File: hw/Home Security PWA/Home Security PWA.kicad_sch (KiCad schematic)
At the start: 52 parts, among them J1 Conn_01x10_Pin, J10 1825960000, J11 1825960000, J12 1825960000, J13 1825960000, J14 1825960000, J15 1825960000, J16 1825960000, J17 1825960000, J18 1825960000, J19 1825960000, J2 Conn_01x10_Pin, J20 1825960000, J21 1825960000, J22 1825960000, J23 1825960000, J24 1825960000, J25 1825960000, J26 1825960000, J27 1825960000, J28 1825960000, J29 1825960000, J3 1825960000, J30 1825960000, J31 1825960000, J32 1825960000, J33 1825960000, J34 1825960000, J4 1825960000, J5 1825960000, J6 1825960000, J7 1825960000, J8 1825960000, J9 1825960000, U1 ADS1115IDGS, U2 ADS1115IDGS, U3 MCP23017_SO

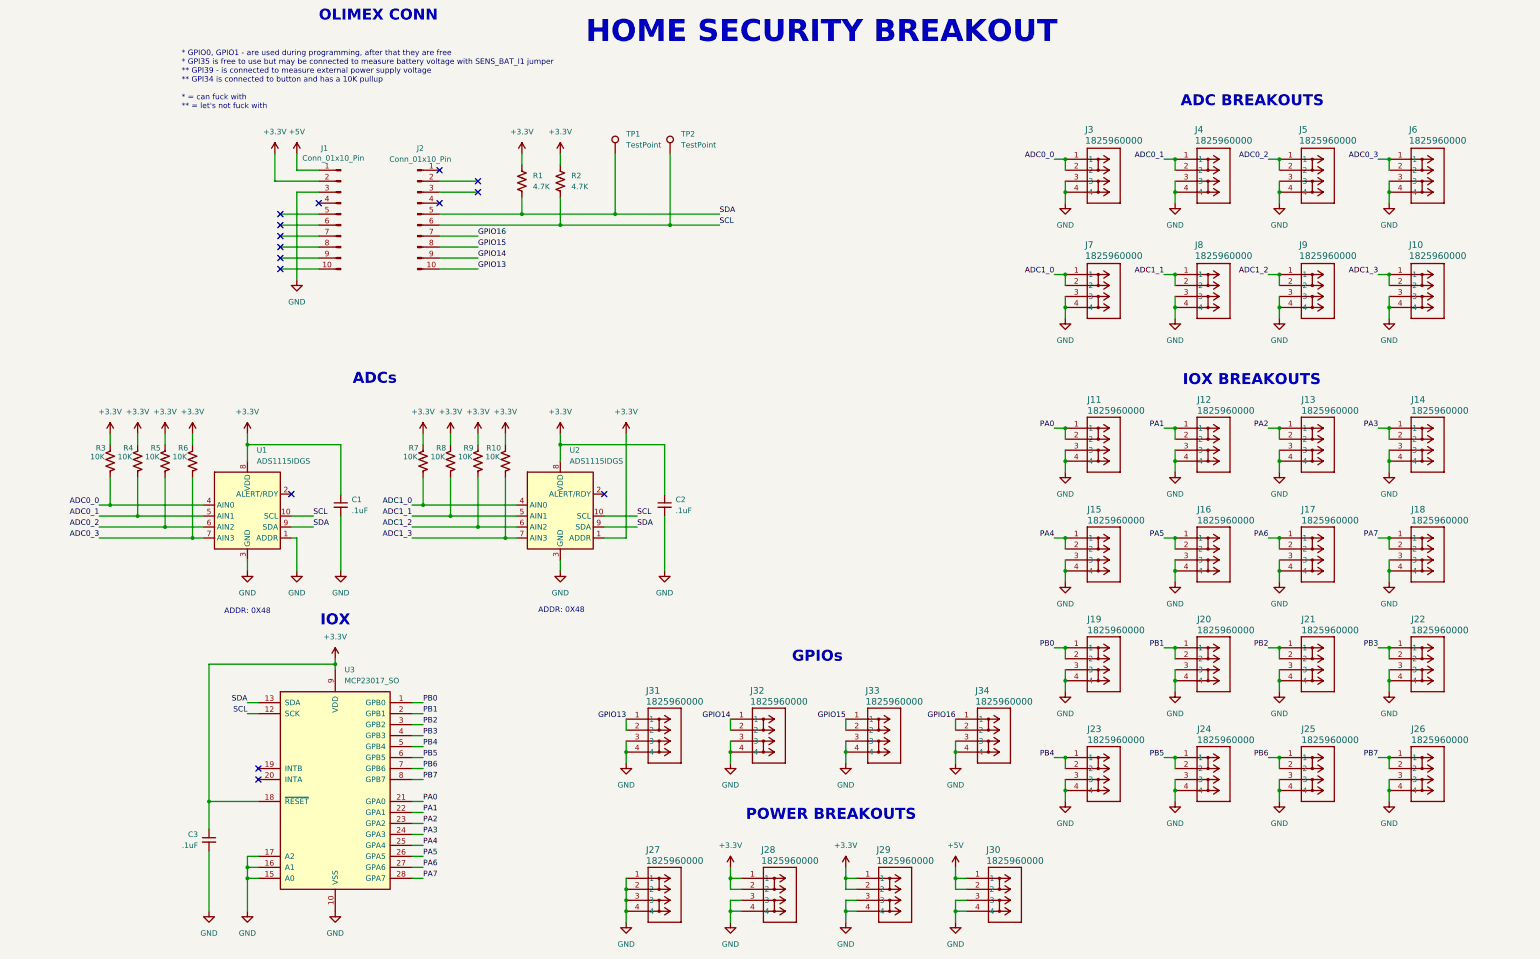
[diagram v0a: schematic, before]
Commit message: Remove these "per project" components.
Updates to Home Security with Inventree, new symbols, new schematics.
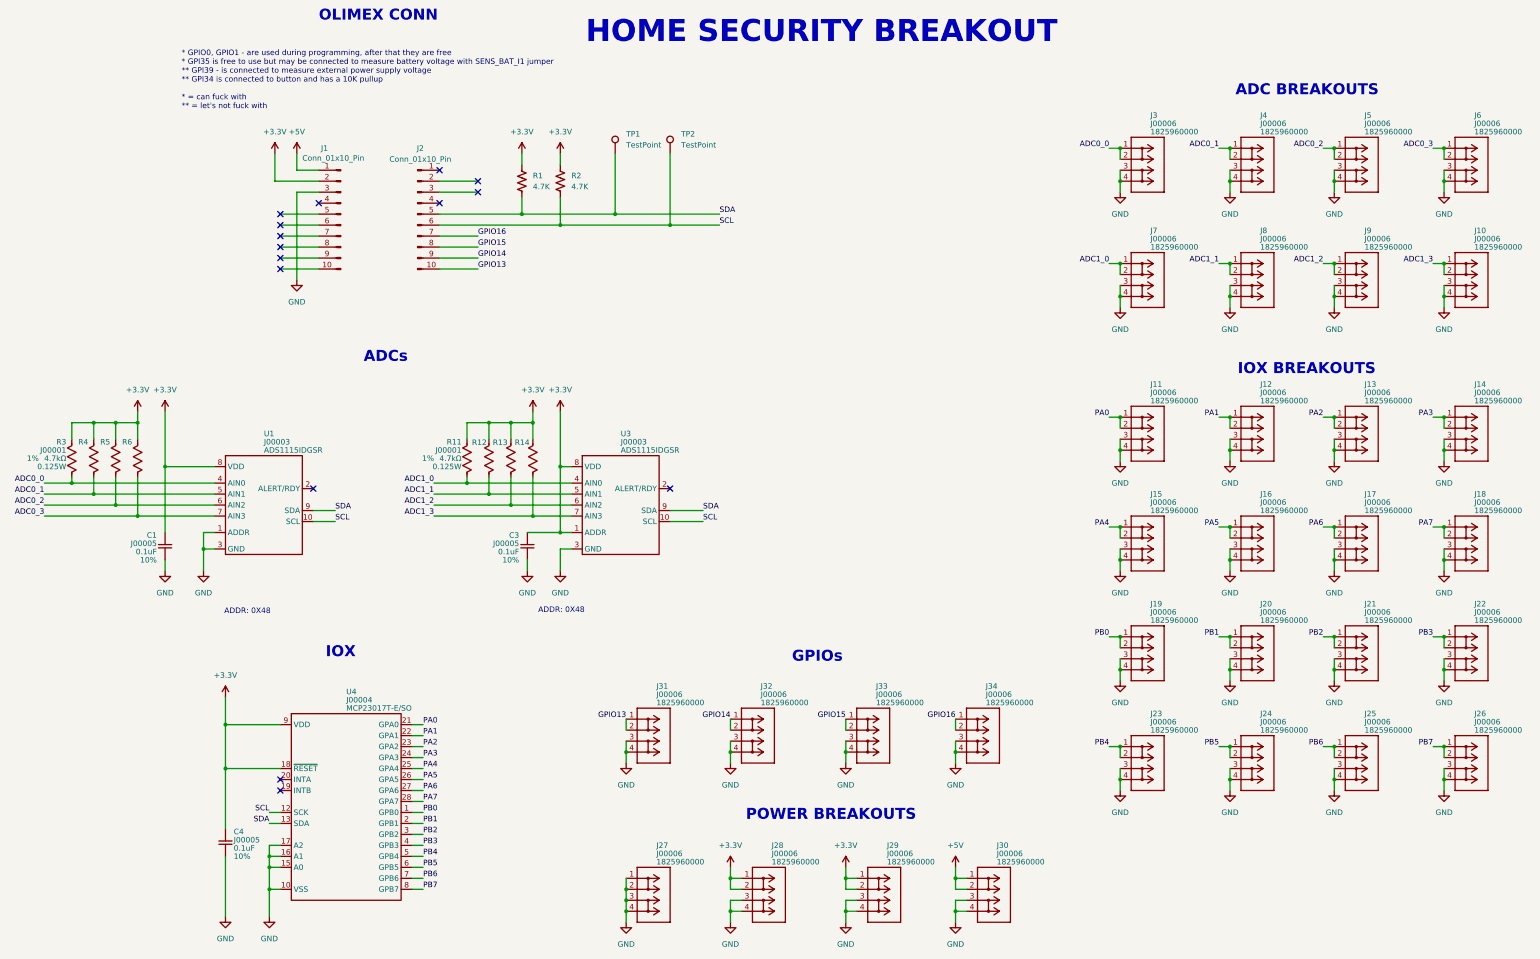
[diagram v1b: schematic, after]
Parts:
- removed C1, C2, C3: .1uF, Capacitor_SMD:C_0805_2012Metric_Pad1.18x1.45mm_HandSolder, symbol Device:C_Small
- removed R10, R7, R8, R9: 10K, Resistor_SMD:R_0805_2012Metric_Pad1.20x1.40mm_HandSolder, symbol Device:R_US
- removed U1, U2: ADS1115IDGS, Package_SO:TSSOP-10_3x3mm_P0.5mm, symbol Analog_ADC:ADS1115IDGS
- removed U3: MCP23017_SO, Package_SO:SOIC-28W_7.5x17.9mm_P1.27mm, symbol Interface_Expansion:MCP23017_SO
- added C1, C3, C4: J00005, JLibrary:CAPC201X125X100L50M, symbol JLibrary_inventree:J00005
- added R11, R12, R13, R14: J00001, JLibrary:RESC2012X60M, symbol JLibrary_inventree:J00001
- added U1, U3: J00003, JLibrary:SOP10P50_300X490X110L55X22M, symbol JLibrary_inventree:J00003
- added U4: J00004, JLibrary:SOIC127P1030X265-28M, symbol JLibrary_inventree:J00004
- J10, J11, J12, J13, J14, J15, J16, J17, J18, J19, J20, J21, J22, J23, J24, J25, J26, J27, J28, J29, J3, J30, J31, J32, J33, J34, J4, J5, J6, J7, J8, J9: value 1825960000 -> J00006; footprint footprint:CONN_1825960000_WED -> JLibrary:J00006; symbol 1825960000:1825960000 -> JLibrary_inventree:J00006; Current (none) -> 12A; Gender (none) -> Female; InvenTree (none) -> 20; MPN_1 (none) -> 1825960000; Manufacturer_1 (none) -> Weidmüller; Mount (none) -> TH; Orientation (none) -> Vertical; Part URL (none) -> https://inventree.justyn.party/web/part/20/; Pin Arrangement (none) -> 1x2; SPN_1_1 (none) -> 281-2124-ND; Supplier_1_1 (none) -> Digikey; TMax (none) -> 120C; TMin (none) -> -50C; Voltage (none) -> 300V
- R3, R4, R5, R6: value 10K -> J00001; footprint Resistor_SMD:R_0805_2012Metric_Pad1.20x1.40mm_HandSolder -> JLibrary:RESC2012X60M; symbol Device:R_US -> JLibrary_inventree:J00001; InvenTree (none) -> 15; MPN_1 (none) -> CRCW08054K70FKEAC; Manufacturer_1 (none) -> Vishay Dale; Mount (none) -> SM; Package (none) -> 0805; Part URL (none) -> https://inventree.justyn.party/web/part/15/; Power (none) -> 0.125W; Resistance (none) -> 4.7kΩ; SPN_1_1 (none) -> 541-4131-1-ND; SPN_1_2 (none) -> 541-4131-2-ND; Supplier_1_1 (none) -> Digikey; Supplier_1_2 (none) -> Digikey; TMax (none) -> 155C; TMin (none) -> -55C; Tolerance (none) -> 1%; Voltage (none) -> 150V
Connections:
- net +3.3V: now also C1.1, C3.1, C4.1, U1.8 (VDD), U3.1 (ADDR), U3.8 (VDD), U4.18 (~{RESET}), U4.9 (VDD); no longer R3.1, R4.1, R5.1, R6.1
- net ADC0_0: now also U1.4 (AIN0); no longer R3.2
- net ADC0_1: now also U1.5 (AIN1); no longer R4.2
- net ADC0_2: now also U1.6 (AIN2); no longer R5.2
- net ADC0_3: now also U1.7 (AIN3); no longer R6.2
- net ADC1_0: now also U3.4 (AIN0)
- net ADC1_1: now also U3.5 (AIN1)
- net ADC1_2: now also U3.6 (AIN2)
- net ADC1_3: now also U3.7 (AIN3)
- net GND: now also C1.2, C3.2, C4.2, U1.1 (ADDR), U1.3 (GND), U3.3 (GND), U4.10 (VSS), U4.15 (A0), U4.16 (A1), U4.17 (A2)
- net PA0: now also U4.21 (GPA0)
- net PA1: now also U4.22 (GPA1)
- net PA2: now also U4.23 (GPA2)
- net PA3: now also U4.24 (GPA3)
- net PA4: now also U4.25 (GPA4)
- net PA5: now also U4.26 (GPA5)
- net PA6: now also U4.27 (GPA6)
- net PA7: now also U4.28 (GPA7)
- net PB0: now also U4.1 (GPB0)
- net PB1: now also U4.2 (GPB1)
- net PB2: now also U4.3 (GPB2)
- net PB3: now also U4.4 (GPB3)
- net PB4: now also U4.5 (GPB4)
- net PB5: now also U4.6 (GPB5)
- net PB6: now also U4.7 (GPB6)
- net PB7: now also U4.8 (GPB7)
- net SCL: now also U1.10 (SCL), U3.10 (SCL), U4.12 (SCK)
- net SDA: now also U1.9 (SDA), U3.9 (SDA), U4.13 (SDA)

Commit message: More work.
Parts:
- removed J1, J2: Conn_01x10_Pin, footprint:PPTC101LFBN-RC, symbol Connector:Conn_01x10_Pin
- added J21, J22: J00007, JLibrary:RHDRV10W64P254_10X1_2590X254H850, symbol JLibrary_inventree:J00007
- added U4: J00008, JLibrary:J00008, symbol JLibrary_inventree:J00008
- renumbered C3 to C1, C4 to C2, C1 to C3, J11 to J1, J20 to J10, J21 to J11, J22 to J12, J23 to J13, J24 to J14, J25 to J15, J26 to J16, J31 to J17, J32 to J18, J33 to J19, J12 to J2, J34 to J20, J3 to J23, J4 to J24, J5 to J25, J6 to J26, J7 to J27, J8 to J28, J9 to J29, J13 to J3, J10 to J30, J28 to J31, J29 to J32, J30 to J33, J27 to J34, J14 to J4, J15 to J5, J16 to J6, J17 to J7, J18 to J8, J19 to J9, R14 to R1, R2 to R10, R13 to R2, R12 to R3, R11 to R4, R6 to R5, R5 to R6, R4 to R7, R3 to R8, R1 to R9, U4 to U2
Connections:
- net +3.3V: now also J21.2
- net +5V: now also J21.1
- net GND: now also J21.3
- net GPIO13: now also J22.10
- net GPIO14: now also J22.9
- net GPIO15: now also J22.8
- net GPIO16: now also J22.7
- net SCL: now also J22.6
- net SDA: now also J22.5
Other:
- note removed: "* GPIO0, GPIO1 - are used during programming, after that they are free * GPI35 is free to use but may be connected to measure battery voltage with SENS_BAT_I1 jumper ** GPI39 - is connected to measure external power supply voltage ** GPI34 is connected to button and has a 10K pullup * = can fuck with ** = let's not fuck with"
- moved on the sheet: C1, C2, C3, J1, J10, J11, J12, J13, J14, J15, J16, J2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

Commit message: Using all custom symbols/footprints.
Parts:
- removed R1, R2, R3, R4, R5, R6, R7, R8: J00001, JLibrary:RESC2012X60M, symbol JLibrary_inventree:J00001
- removed R10, R9: 4.7K, Resistor_SMD:R_0805_2012Metric_Pad1.20x1.40mm_HandSolder, symbol Device:R_US
- removed TP1, TP2: TestPoint, TestPoint:TestPoint_THTPad_D2.0mm_Drill1.0mm, symbol Connector:TestPoint
- added FID1, FID2, FID3: ~, JLibrary:FIDUCIAL_1MM, symbol JLibrary_Generics:FIDUCIAL
- added R1, R2, R3, R4, R5, R6, R7, R8: J00009, JLibrary:RESC2012X60M, symbol JLibrary_inventree:J00009
- added R10, R9: J00001, JLibrary:RESC2012X60M, symbol JLibrary_inventree:J00001
- added TP1, TP2: ~, JLibrary:TESTPOINT_TH_1MMD, symbol JLibrary_Generics:TESTPOINT_1MMD
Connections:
- net ADC0_0: now also R8.1
- net ADC0_1: now also R7.1
- net ADC0_2: now also R6.1
- net ADC0_3: now also R5.1
- net ADC1_0: now also R4.1
- net ADC1_1: now also R3.1
- net ADC1_2: now also R2.1
- net ADC1_3: now also R1.1
- net SCL: now also R10.1, TP2.1
- net SDA: now also R9.1, TP1.1
- no-connect marks 15 -> 18
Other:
- moved on the sheet: C1, C2, C3, J17, J18, J19, J20, J31, J32, J33, J34

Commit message: Updates.
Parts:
- C1, C2, C3: SPN_1 478-KGM21NR71E104KTCT-ND -> (none); SPN_1_1 (none) -> 478-KGM21NR71E104KTCT-ND; SPN_1_2 (none) -> 478-KGM21NR71E104KTTR-ND; SPN_2 478-KGM21NR71E104KTTR-ND -> (none); Supplier_1 Digikey -> (none); Supplier_1_1 (none) -> Digikey; Supplier_1_2 (none) -> Digikey; Supplier_2 Digikey -> (none)
- U1, U3: SPN_1 296-38849-1-ND -> (none); SPN_1_1 (none) -> 296-38849-1-ND; SPN_1_2 (none) -> 296-38849-2-ND; SPN_2 296-38849-2-ND -> (none); Supplier_1 Digikey -> (none); Supplier_1_1 (none) -> Digikey; Supplier_1_2 (none) -> Digikey; Supplier_2 Digikey -> (none)
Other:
- note added: "ADDR: 0X49"
